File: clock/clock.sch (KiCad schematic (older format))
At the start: 4 parts

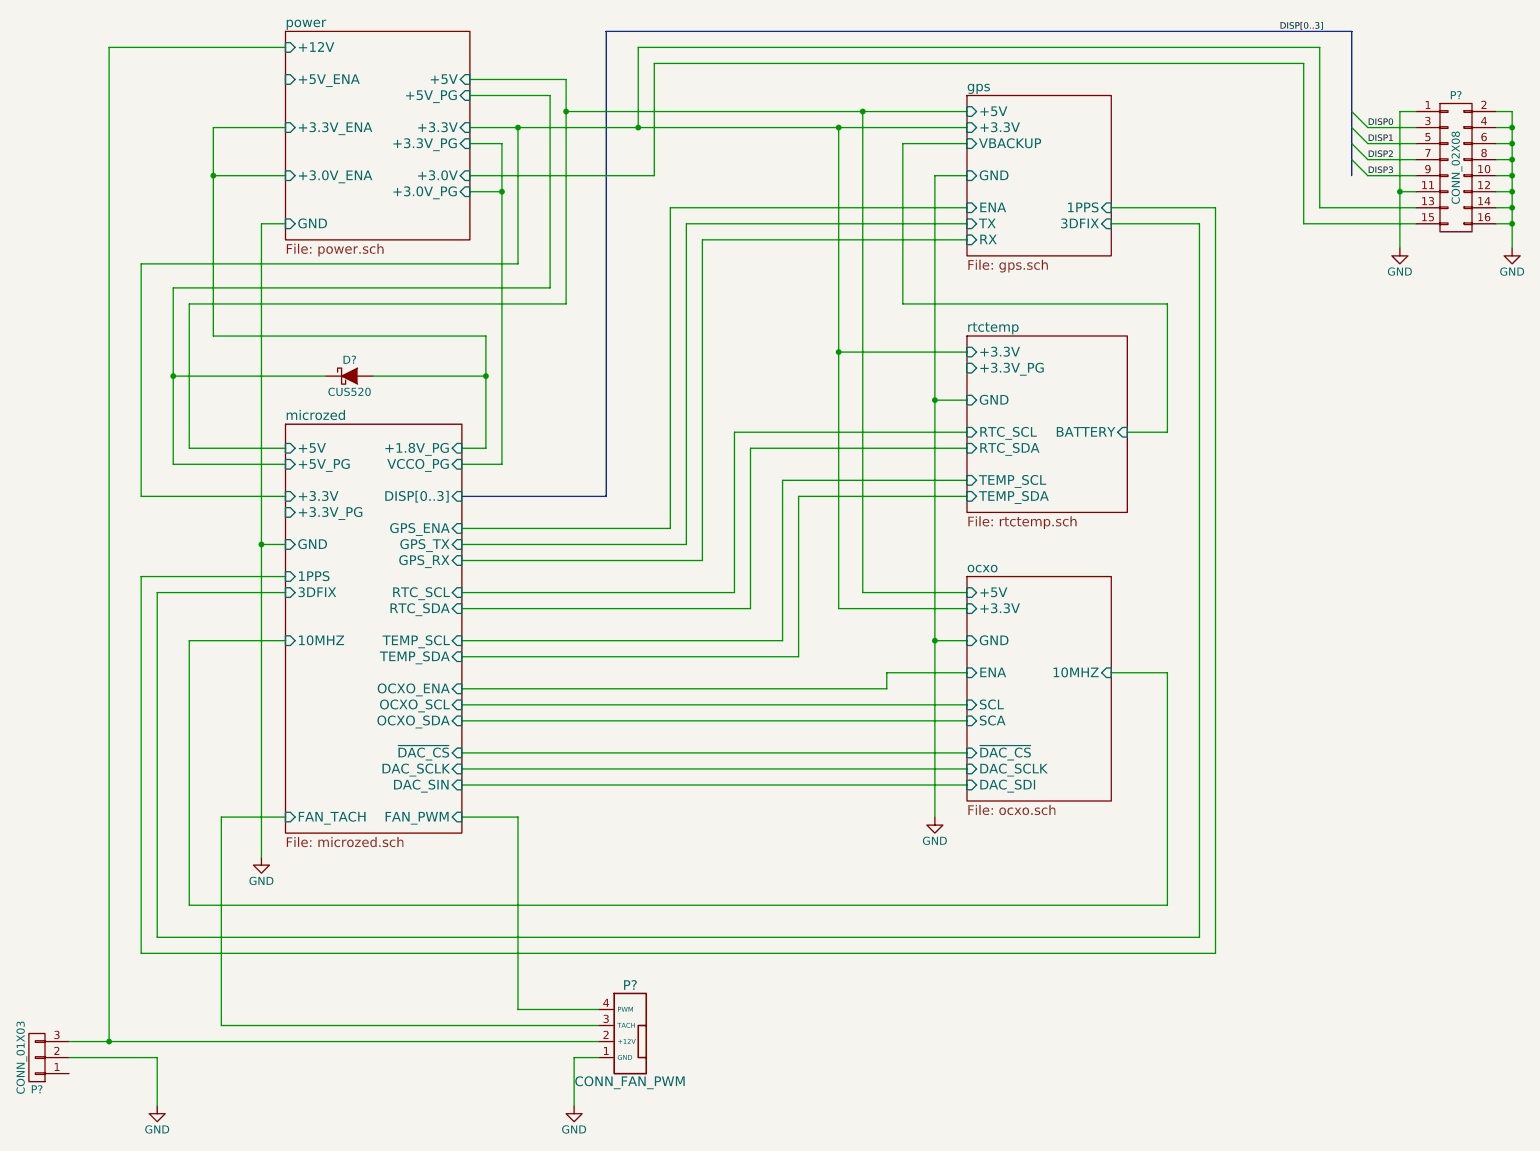
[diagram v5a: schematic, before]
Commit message: Correct footprint selection. Start pcb. Add BOM files.
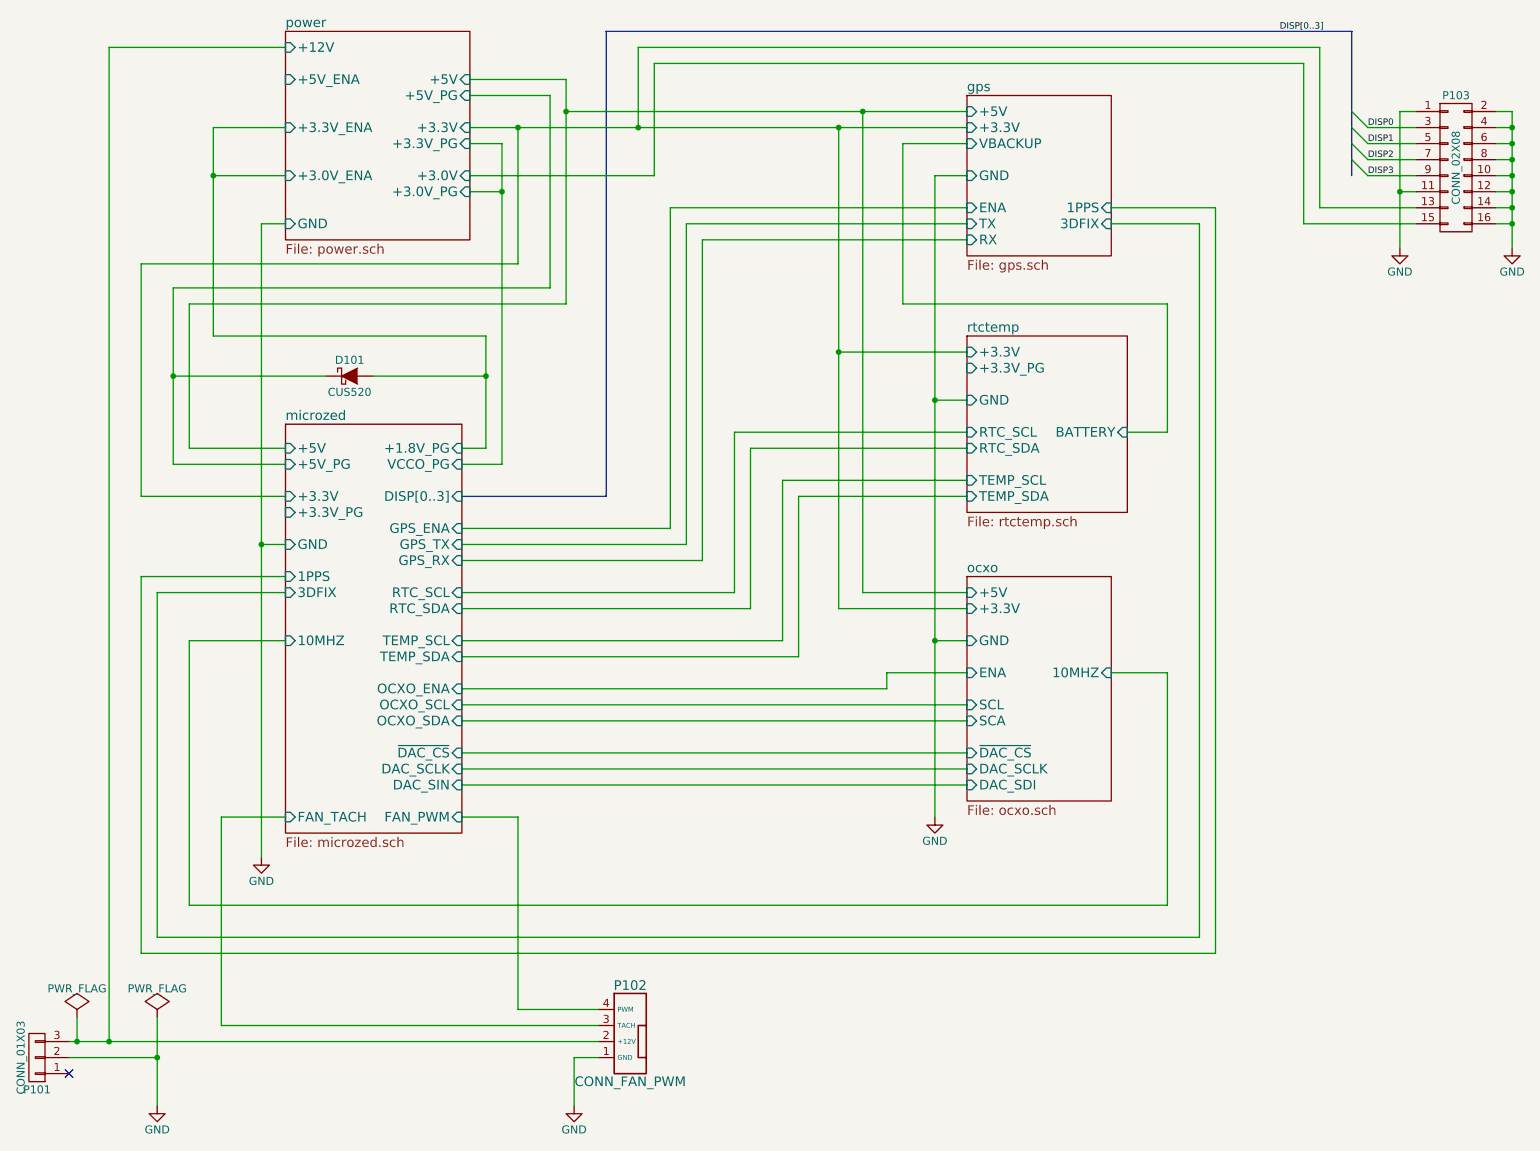
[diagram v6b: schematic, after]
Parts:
- D101: renamed from D?; footprint (none) -> local:CUS520_USC
- P101: renamed from P?; footprint (none) -> local:Terminal_Block_1x03
- P102: renamed from P?; footprint (none) -> local:CONN_47053
- P103: renamed from P?; footprint (none) -> Connect:he10-16d
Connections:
- no-connect marks 0 -> 1
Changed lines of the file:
@@
 Connection ~ 6450 4400
 $Comp
-L GND #PWR?
+L GND #PWR01
 U 1 1 562606B5
 P 6450 5500
-F 0 "#PWR?" H 6450 5250 50  0001 C CNN
+F 0 "#PWR01" H 6450 5250 50  0001 C CNN
 F 1 "GND" H 6450 5350 50  0000 C CNN
 F 2 "" H 6450 5500 60  0000 C CNN
@@
 $EndComp
 $Comp
-L GND #PWR?
+L GND #PWR02
 U 1 1 562607ED
 P 2250 5750
-F 0 "#PWR?" H 2250 5500 50  0001 C CNN
+F 0 "#PWR02" H 2250 5500 50  0001 C CNN
 F 1 "GND" H 2250 5600 50  0000 C CNN
 F 2 "" H 2250 5750 60  0000 C CNN
@@
 	1700 3300 2400 3300
 $Comp
-L D_Schottky D?
+L D_Schottky D101
 U 1 1 56266B0B
 P 2800 2750
-F 0 "D?" H 2800 2850 50  0000 C CNN
+F 0 "D101" H 2800 2850 50  0000 C CNN
 F 1 "CUS520" H 2800 2650 50  0000 C CNN
-F 2 "" H 2800 2750 60  0000 C CNN
+F 2 "local:CUS520_USC" H 2800 2750 60  0001 C CNN
 F 3 "" H 2800 2750 60  0000 C CNN
 F 4 "Toshiba" H 2800 2750 50  0001 C CNN "Manufacturer"
@@
 $EndSheet
 $Comp
-L CONN_02X08 P?
+L CONN_02X08 P103
 U 1 1 5632C7F9
 P 9700 1450
-F 0 "P?" H 9700 1900 50  0000 C CNN
+F 0 "P103" H 9700 1900 50  0000 C CNN
 F 1 "CONN_02X08" V 9700 1450 50  0000 C CNN
-F 2 "" H 9700 250 60  0000 C CNN
+F 2 "Connect:he10-16d" H 9700 250 60  0001 C CNN
 F 3 "" H 9700 250 60  0000 C CNN
 	1    9700 1450
@@
 $EndComp
 $Comp
-L GND #PWR?
+L GND #PWR03
 U 1 1 5632D32A
 P 10050 1950
-F 0 "#PWR?" H 10050 1700 50  0001 C CNN
+F 0 "#PWR03" H 10050 1700 50  0001 C CNN
 F 1 "GND" H 10050 1800 50  0000 C CNN
 F 2 "" H 10050 1950 60  0000 C CNN
@@
 Connection ~ 10050 1200
 $Comp
-L GND #PWR?
+L GND #PWR04
 U 1 1 5632E81A
 P 9350 1950
-F 0 "#PWR?" H 9350 1700 50  0001 C CNN
+F 0 "#PWR04" H 9350 1700 50  0001 C CNN
 F 1 "GND" H 9350 1800 50  0000 C CNN
 F 2 "" H 9350 1950 60  0000 C CNN
@@
 Connection ~ 4150 1100
 $Comp
-L CONN_FAN_PWM P?
+L CONN_FAN_PWM P102
 U 1 1 563D6A73
 P 4550 6850
-F 0 "P?" H 4550 7150 60  0000 C CNN
+F 0 "P102" H 4550 7150 60  0000 C CNN
 F 1 "CONN_FAN_PWM" H 4550 6550 60  0000 C CNN
-F 2 "" H 4750 6800 60  0000 C CNN
+F 2 "local:CONN_47053" H 4750 6800 60  0001 C CNN
 F 3 "" H 4750 6800 60  0000 C CNN
 F 4 "Molex" H 4550 7350 50  0001 C CNN "Manufacturer"
@@
 	2000 5500 2400 5500
 $Comp
-L GND #PWR?
+L GND #PWR05
 U 1 1 563D71E9
 P 4200 7300
-F 0 "#PWR?" H 4200 7050 50  0001 C CNN
+F 0 "#PWR05" H 4200 7050 50  0001 C CNN
 F 1 "GND" H 4200 7150 50  0000 C CNN
 F 2 "" H 4200 7300 60  0000 C CNN
@@
 	1050 6900 4350 6900
 $Comp
-L CONN_01X03 P?
+L CONN_01X03 P101
 U 1 1 563D5B9B
 P 850 7000
-F 0 "P?" H 850 7200 50  0000 C CNN
+F 0 "P101" H 850 7200 50  0000 C CNN
 F 1 "CONN_01X03" V 950 7000 50  0000 C CNN
-F 2 "" H 850 7000 60  0000 C CNN
+F 2 "local:Terminal_Block_1x03" H 850 7000 60  0001 C CNN
 F 3 "" H 850 7000 60  0000 C CNN
 	1    850  7000
@@
 	1050 7000 1600 7000
 Wire Wire Line
-	1600 7000 1600 7300
-$Comp
-L GND #PWR?
+	1600 6750 1600 7300
+$Comp
+L GND #PWR06
 U 1 1 563D694B
 P 1600 7300
-F 0 "#PWR?" H 1600 7050 50  0001 C CNN
+F 0 "#PWR06" H 1600 7050 50  0001 C CNN
 F 1 "GND" H 1600 7150 50  0000 C CNN
 F 2 "" H 1600 7300 60  0000 C CNN
@@
 	1    0    0    -1
 $EndComp
+NoConn ~ 1050 7100
+$Comp
+L PWR_FLAG #FLG07
+U 1 1 563DBCC7
+P 1600 6750
+F 0 "#FLG07" H 1600 6845 50  0001 C CNN
+F 1 "PWR_FLAG" H 1600 6930 50  0000 C CNN
+F 2 "" H 1600 6750 60  0000 C CNN
+F 3 "" H 1600 6750 60  0000 C CNN
+	1    1600 6750
+	1    0    0    -1
+$EndComp
+$Comp
+L PWR_FLAG #FLG08
+U 1 1 563DC9E1
+P 1100 6750
+F 0 "#FLG08" H 1100 6845 50  0001 C CNN
+F 1 "PWR_FLAG" H 1100 6930 50  0000 C CNN
+F 2 "" H 1100 6750 60  0000 C CNN
+F 3 "" H 1100 6750 60  0000 C CNN
+	1    1100 6750
+	1    0    0    -1
+$EndComp
+Wire Wire Line
+	1100 6750 1100 6900
+Connection ~ 1100 6900
+Connection ~ 1600 7000
 $EndSCHEMATC

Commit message: Checkpoint PCB.
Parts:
- D101: footprint local:CUS520_USC -> local:SOD-323_USC
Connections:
- net power/+12V: now also P101.1 (P1); no longer P101.3 (P3)
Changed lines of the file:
@@
 F 0 "D101" H 2800 2850 50  0000 C CNN
 F 1 "CUS520" H 2800 2650 50  0000 C CNN
-F 2 "local:CUS520_USC" H 2800 2750 60  0001 C CNN
+F 2 "local:SOD-323_USC" H 2800 2750 60  0001 C CNN
 F 3 "" H 2800 2750 60  0000 C CNN
 F 4 "Toshiba" H 2800 2750 50  0001 C CNN "Manufacturer"
@@
 	1    0    0    -1
 $EndComp
-NoConn ~ 1050 7100
+NoConn ~ 1050 6900
 $Comp
 L PWR_FLAG #FLG07
@@
 L PWR_FLAG #FLG08
 U 1 1 563DC9E1
-P 1100 6750
-F 0 "#FLG08" H 1100 6845 50  0001 C CNN
-F 1 "PWR_FLAG" H 1100 6930 50  0000 C CNN
-F 2 "" H 1100 6750 60  0000 C CNN
-F 3 "" H 1100 6750 60  0000 C CNN
-	1    1100 6750
+P 2400 6750
+F 0 "#FLG08" H 2400 6845 50  0001 C CNN
+F 1 "PWR_FLAG" H 2400 6930 50  0000 C CNN
+F 2 "" H 2400 6750 60  0000 C CNN
+F 3 "" H 2400 6750 60  0000 C CNN
+	1    2400 6750
 	1    0    0    -1
 $EndComp
@@
 	2400 700  1300 700
 Wire Wire Line
-	1300 700  1300 6900
-Wire Wire Line
-	1050 6900 4350 6900
+	1300 700  1300 7100
 Connection ~ 1300 6900
 Wire Wire Line
@@
 	1600 6750 1600 7300
 Wire Wire Line
-	1100 6750 1100 6900
-Connection ~ 1100 6900
+	2400 6750 2400 6900
+Connection ~ 2400 6900
 Connection ~ 1600 7000
+Wire Wire Line
+	1300 6900 4350 6900
+Wire Wire Line
+	1300 7100 1050 7100
 $EndSCHEMATC
